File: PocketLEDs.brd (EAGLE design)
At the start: 25.8 x 21.1 mm, 14 parts, among them J1 AVR_SPI_PRG_6PTH, U1 ATMEGA328P-MU, Y1 16MHZ

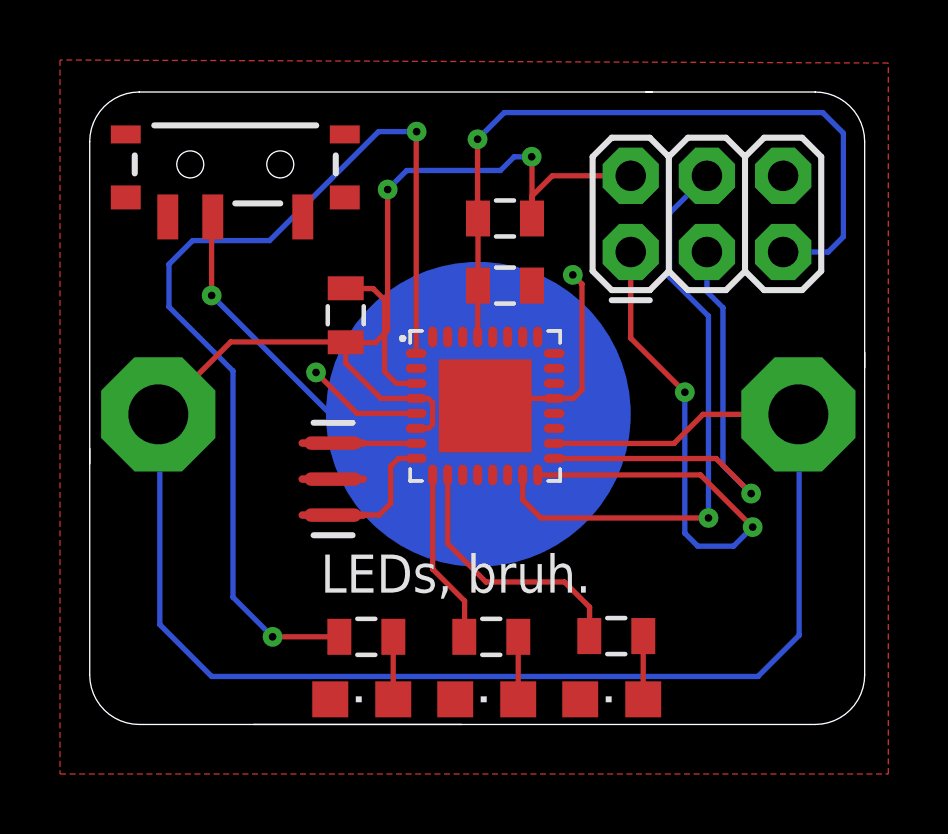
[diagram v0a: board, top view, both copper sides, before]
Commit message: Fixed GND traces
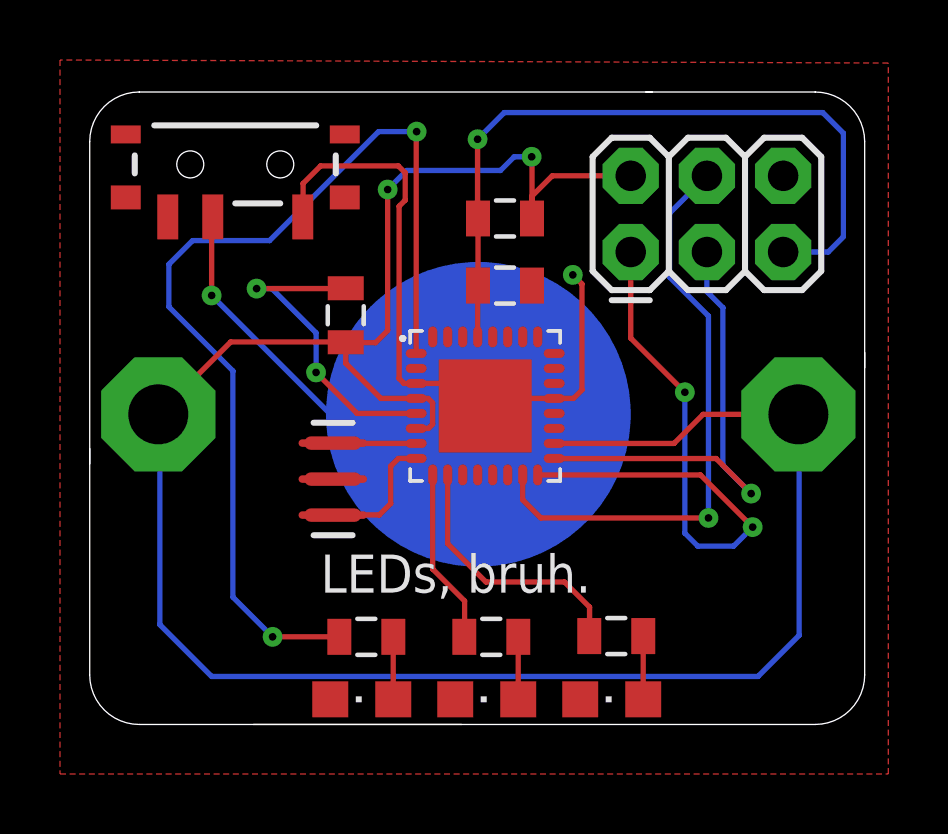
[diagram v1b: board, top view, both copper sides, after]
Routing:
- net GND: track 16.4 -> 33.3 mm, vias 2 -> 3
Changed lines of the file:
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@@
 <wire x1="10.8826" y1="9.5798" x2="8.9114" y2="9.5798" width="0.1778" layer="1"/>
 <wire x1="8.9114" y1="9.5798" x2="7.5438" y2="10.9474" width="0.1778" layer="1"/>
-<wire x1="10.8826" y1="10.5798" x2="10.2228" y2="10.5798" width="0.1778" layer="1"/>
-<wire x1="10.2228" y1="10.5798" x2="9.8298" y2="10.9728" width="0.1778" layer="1"/>
-<wire x1="9.8298" y1="10.9728" x2="9.8298" y2="13.3604" width="0.1778" layer="1"/>
-<wire x1="9.8298" y1="13.3604" x2="9.4488" y2="13.7414" width="0.1778" layer="1"/>
-<wire x1="9.4488" y1="13.7414" x2="8.5454" y2="13.7414" width="0.1778" layer="1"/>
 <wire x1="8.5454" y1="13.7414" x2="8.5344" y2="13.7524" width="0.1778" layer="1"/>
 <via x="16.1036" y="14.1986" extent="1-16" drill="0.254" diameter="0.127"/>
@@
 <wire x1="15.4826" y1="10.0798" x2="13.4326" y2="10.0798" width="0.1778" layer="1"/>
 <wire x1="13.4326" y1="10.0798" x2="13.1826" y2="9.8298" width="0.1778" layer="1"/>
-<wire x1="10.8826" y1="10.5798" x2="10.8826" y2="9.5798" width="0" layer="19" extent="1-1"/>
-<wire x1="13.1826" y1="9.8298" x2="10.8826" y2="9.5798" width="0" layer="19" extent="1-1"/>
+<wire x1="10.8826" y1="10.5798" x2="12.4326" y2="10.5798" width="0.1778" layer="1"/>
+<wire x1="12.4326" y1="10.5798" x2="13.1826" y2="9.8298" width="0.1778" layer="1"/>
+<wire x1="8.5454" y1="13.7414" x2="5.5626" y2="13.7414" width="0.1778" layer="1"/>
+<via x="5.5626" y="13.7414" extent="1-16" drill="0.254" diameter="0.127"/>
+<wire x1="5.5626" y1="13.7414" x2="6.0706" y2="13.7414" width="0.1778" layer="16"/>
+<wire x1="6.0706" y1="13.7414" x2="7.5438" y2="12.2682" width="0.1778" layer="16"/>
+<wire x1="7.5438" y1="12.2682" x2="7.5438" y2="10.9474" width="0.1778" layer="16"/>
+<wire x1="10.8826" y1="10.5798" x2="10.4768" y2="10.5798" width="0.1778" layer="1"/>
+<wire x1="10.4768" y1="10.5798" x2="10.3124" y2="10.7442" width="0.1778" layer="1"/>
+<wire x1="10.3124" y1="10.7442" x2="10.3124" y2="16.4846" width="0.1778" layer="1"/>
+<wire x1="10.3124" y1="16.4846" x2="10.5156" y2="16.6878" width="0.1778" layer="1"/>
+<wire x1="10.5156" y1="16.6878" x2="10.5156" y2="17.6022" width="0.1778" layer="1"/>
+<wire x1="10.5156" y1="17.6022" x2="10.287" y2="17.8308" width="0.1778" layer="1"/>
+<wire x1="10.287" y1="17.8308" x2="7.6962" y2="17.8308" width="0.1778" layer="1"/>
+<wire x1="7.6962" y1="17.8308" x2="7.112" y2="17.2466" width="0.1778" layer="1"/>
+<wire x1="7.112" y1="17.2466" x2="7.112" y2="16.1422" width="0.1778" layer="1"/>
+<wire x1="7.112" y1="16.1422" x2="7.1014" y2="16.1316" width="0.1778" layer="1"/>
 </signal>
 <signal name="SS">
